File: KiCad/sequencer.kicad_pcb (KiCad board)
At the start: 2 copper layers, 79.9 x 100 mm, 125 parts, among them J1 CLOCK OUT, J2 GATE OUT, J3 CLOCK IN, J4 CV OUT, J5 RESET, J6 10-pin power header, Q1 BC848W, Q2 MMBT3904, Q3 MMBT3904, Q4 MMBT3904, Q5 MMBT3904, Q6 MMBT3904, Q7 MMBT3904, Q8 MMBT3904, Q9 MMBT3904, SW1 SW_Nidec_CAS-120A1, SW2 Step1, U1 TL074, U2 CD4017BE

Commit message: placing layout frontview
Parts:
- RV10, RV11, RV3, RV4, RV5, RV6, RV7, RV8, RV9: footprint Eurorack:RD901F -> Eurorack:RD901F_1
- SW2: value Step1 -> ~
- moved J1 48.1 mm to (118.5, 117.3), turned to 180 degrees
- moved J5 23.2 mm to (62.6, 132.0), turned to 180 degrees
- moved J6 22.6 mm to (85.9, 71.0)
- moved U1 20.7 mm to (84.0, 107.8)
- moved J2 18.6 mm to (118.5, 132.0), turned to 180 degrees
- moved RV1 16.7 mm to (102.8, 106.3), turned to -90 degrees
- moved U2 15.0 mm to (61.2, 113.9)
- moved RV2 13.7 mm to (120.4, 106.3), turned to -90 degrees
- moved S1 9.36 mm to (89.1, 133.0)
- moved J3 9.29 mm to (49.4, 132.0), turned to 180 degrees
- moved J4 6.77 mm to (105.3, 132.0), turned to 180 degrees
- moved RV3 6.69 mm to (56.0, 117.2), turned to 90 degrees
- moved SW5 6.62 mm to (112.0, 46.8)
- moved D28 5.85 mm to (110.7, 76.3)
- moved SW7 5.77 mm to (74.7, 105.1)
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
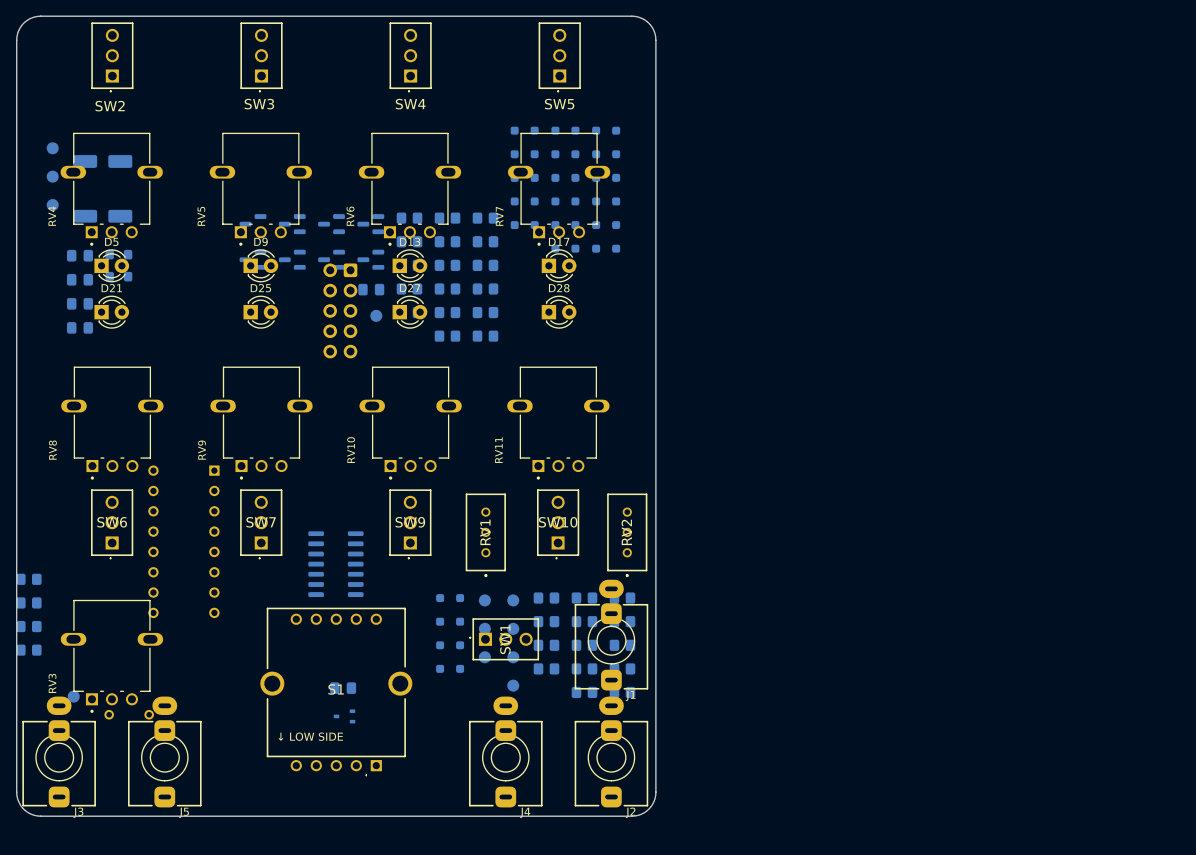
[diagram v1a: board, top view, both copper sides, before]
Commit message: fixing some errors in schematics; first component placement
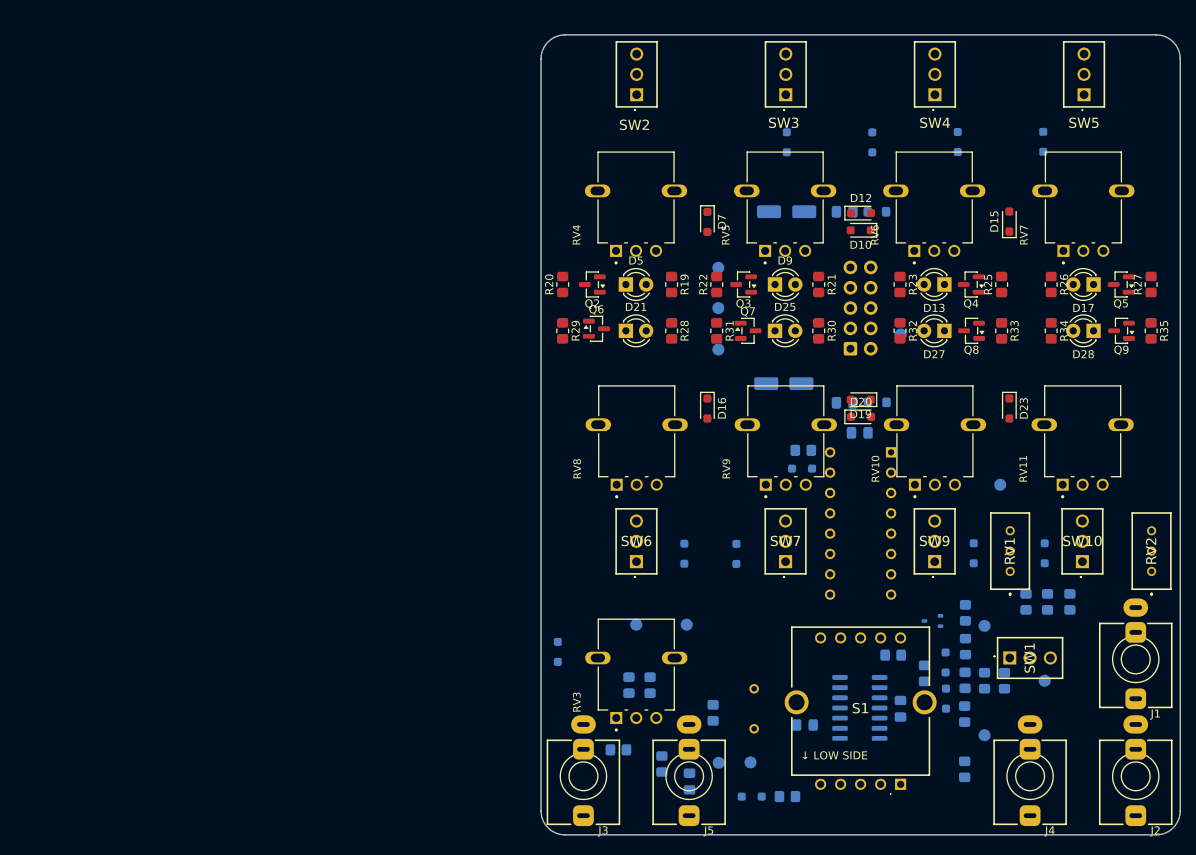
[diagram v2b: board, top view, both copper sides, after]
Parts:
- D10, D12, D15, D16, D19, D20, D23, D7, Q2, Q3, Q4, Q5, Q6, Q7, Q8, Q9, R19, R20, R21, R22, R23, R25, R26, R27, R28, R29, R30, R31, R32, R33, R34, R35: moved to F.Cu
- R13: value 51k -> 18k
- moved C7 114.4 mm to (154.6, 125.9), turned to -90 degrees
- moved Q9 108.9 mm to (182.2, 78.6)
- moved C8 103.3 mm to (142.7, 127.9), turned to 0 degrees
- moved Q5 98.7 mm to (182.2, 72.8)
- moved C5 96.8 mm to (147.6, 87.6)
- moved FB2 96.1 mm to (151.7, 87.6)
- moved C3 95.8 mm to (147.6, 63.7)
- moved FB1 94.9 mm to (151.6, 63.7), turned to 0 degrees
- moved R35 92.7 mm to (185.9, 78.6), turned to -90 degrees
- moved Q8 90.8 mm to (163.5, 78.6)
- moved R27 88.0 mm to (185.9, 72.8), turned to 90 degrees
- moved C6 87.7 mm to (140.0, 85.2), turned to 0 degrees
- moved R15 87.1 mm to (131.2, 126.4), turned to -90 degrees
- moved C4 85.7 mm to (140.4, 63.7)
- moved TP11 85.1 mm to (131.8, 80.9)
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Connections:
- D10 pad 2: GND -> Net-(D10-A)
- D11 pad 2: /CD4017BE/EXTERNAL RESET -> Net-(D11-A)
- D12 pad 2: GND -> Net-(D12-A)
- D15 pad 2: GND -> Net-(D15-A)
- D16 pad 2: GND -> Net-(D16-A)
- D19 pad 2: GND -> Net-(D19-A)
- D20 pad 2: GND -> Net-(D20-A)
- D23 pad 2: GND -> Net-(D23-A)
- FB1 pad 2: Net-(J6-Pin_10) -> +12V
- FB2 pad 2: Net-(J6-Pin_1) -> -12V
- J6 pad 1: Net-(J6-Pin_1) -> -12V
- J6 pad 10: Net-(J6-Pin_10) -> +12V
- J6 pad 2: Net-(J6-Pin_1) -> -12V
- J6 pad 9: Net-(J6-Pin_10) -> +12V
- RV10 pad 2: GND -> Net-(D20-A)
- RV11 pad 2: GND -> Net-(D23-A)
- RV5 pad 2: GND -> Net-(D10-A)
- RV6 pad 2: GND -> Net-(D12-A)
- RV7 pad 2: GND -> Net-(D15-A)
- RV8 pad 2: GND -> Net-(D16-A)
- RV9 pad 2: GND -> Net-(D19-A)
- S1 pad 1: /CD4017BE/EXTERNAL RESET -> Net-(D11-A)
- S1 pad 10: /CD4017BE/EXTERNAL RESET -> Net-(D11-A)

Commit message: connecting all components and adding copper layers, vias tracks…
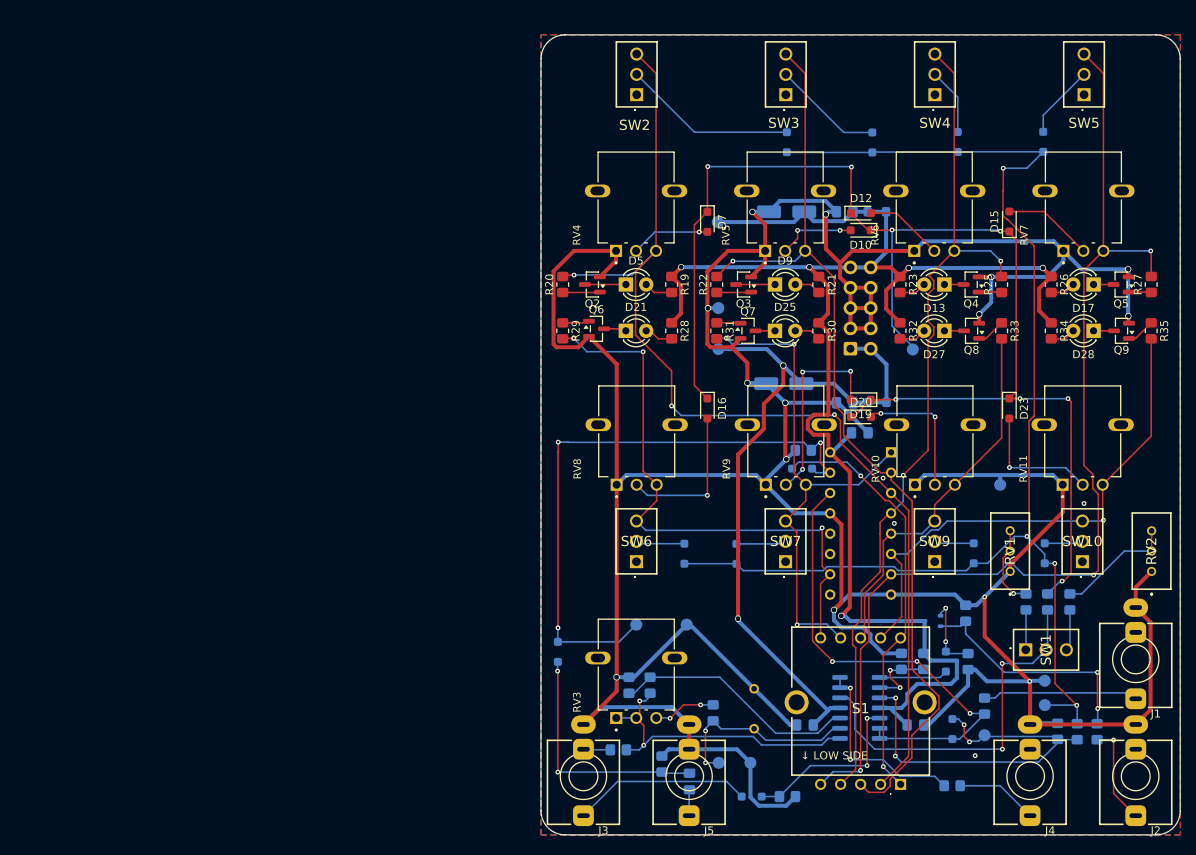
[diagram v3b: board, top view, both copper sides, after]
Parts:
- moved R3 13.2 mm to (179.2, 128.7)
- moved R1 13.2 mm to (176.7, 128.7)
- moved R4 13.2 mm to (174.2, 128.7)
- moved TP2 12.4 mm to (172.6, 125.4)
- moved TP9 5.72 mm to (131.7, 65.0)
- moved D2 3.89 mm to (161.1, 128.4)
- moved C7 2.76 mm to (156.5, 127.9), turned to 0 degrees
- moved R8 2.68 mm to (165.1, 125.5)
- moved R10 2.57 mm to (161.1, 135.5), turned to 180 degrees
- moved TP12 2.41 mm to (156.1, 80.9)
- moved SW1 2.25 mm to (170.3, 118.5)
- moved R6 1.90 mm to (163.0, 120.0), turned to 90 degrees
- moved R2 1.51 mm to (157.5, 119.9), turned to -90 degrees
- moved R5 1.30 mm to (154.7, 119.9), turned to -90 degrees
- moved D1 0.11 mm to (160.3, 120.0)
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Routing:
- net GND: track 0.00 -> 516.2 mm, vias 0 -> 18
- net +12V: track 0.00 -> 193.2 mm, vias 0 -> 5
- net /CD4017BE/CV OUT: track 0.00 -> 168.1 mm, vias 0 -> 8
- net /CD4017BE/GATE OUT: track 0.00 -> 162.3 mm, vias 0 -> 4
- net /CD4017BE/Count3: track 0.00 -> 135.5 mm, vias 0 -> 3
- net /CD4017BE/Count0: track 0.00 -> 133.3 mm, vias 0 -> 3
- net /CD4017BE/Count1: track 0.00 -> 119.7 mm, vias 0 -> 1
- net /CD4017BE/Count2: track 0.00 -> 108.0 mm, vias 0 -> 2
- net -12V: track 0.00 -> 88.2 mm, vias 0 -> 2
- net /CD4017BE/EXTERNAL RESET: track 0.00 -> 76.2 mm, vias 0 -> 3
- net /CD4017BE/Count4: track 0.00 -> 72.2 mm, vias 0 -> 3
- net /CD4017BE/Count5: track 0.00 -> 65.9 mm, vias 0 -> 3
- net /CD4017BE/Count7: track 0.00 -> 65.6 mm, vias 0 -> 1
- net /CD4017BE/EXTERNAL CLOCK: track 0.00 -> 60.5 mm, vias 0 -> 3
- net Net-(D11-A): track 0.00 -> 52.8 mm, vias 0 -> 2
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- added copper zone on B.Cu, net GND
- added copper zone on F.Cu, net GND

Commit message: rerouting and editing silkscreen
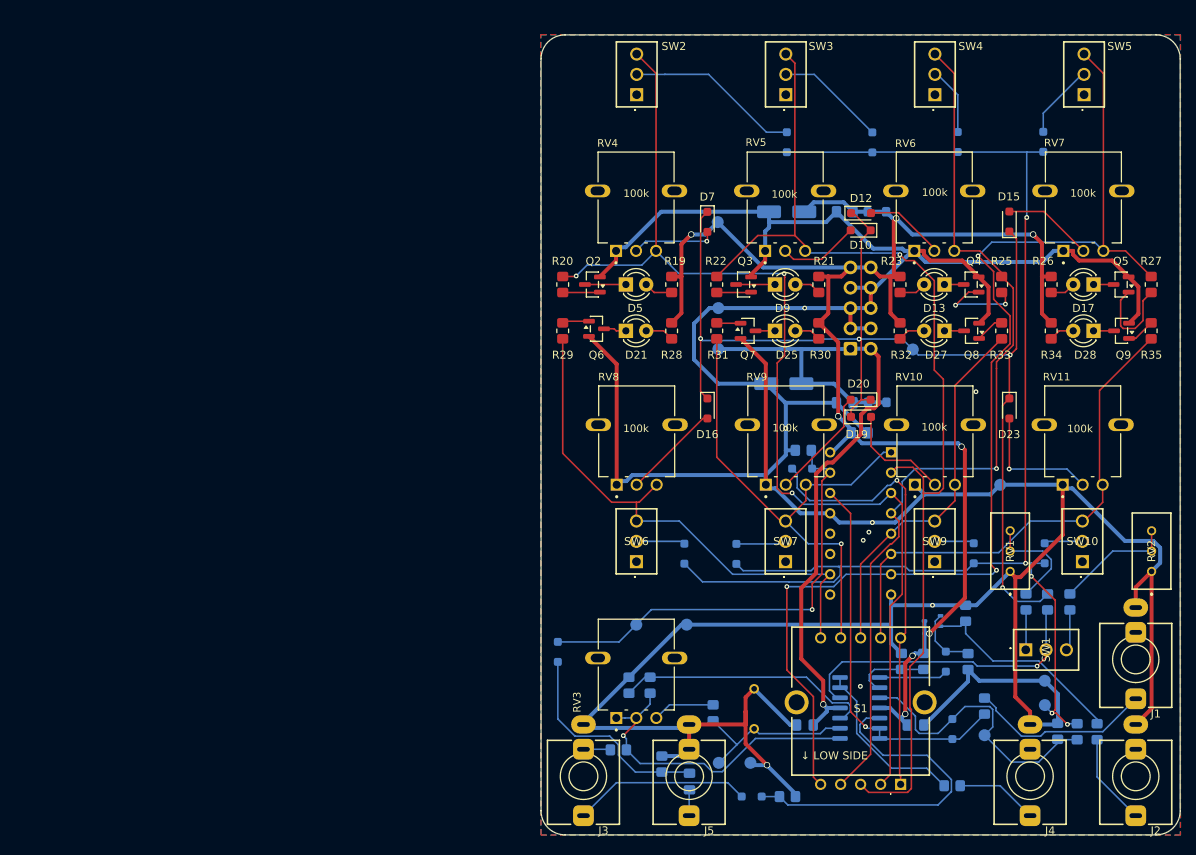
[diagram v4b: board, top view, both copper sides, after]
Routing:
- net /CD4017BE/CV OUT: track 168.1 -> 145.2 mm, vias 8 -> 4
- net Net-(D3-K): track 22.3 -> 44.0 mm, vias 2 -> 0
- net /CD4017BE/EXTERNAL RESET: track 76.2 -> 56.3 mm, vias 3 -> 1
- net /CD4017BE/Count1: track 119.7 -> 136.0 mm
- net Net-(D2-A): track 49.6 -> 36.6 mm, vias 4 -> 0
- net /CD4017BE/EXTERNAL CLOCK: track 60.5 -> 48.6 mm, vias 3 -> 1
- net Net-(D19-A): track 24.7 -> 14.0 mm, vias 3 -> 0
- net /CD4017BE/Count3: track 135.5 -> 145.4 mm
- net Net-(Q4-B): track 2.89 -> 12.3 mm, vias 0 -> 2
- net Net-(Q5-B): track 2.84 -> 11.9 mm
- net /CD4017BE/GATE OUT: track 162.3 -> 171.2 mm, vias 4 -> 5
- net Net-(SW1-B): track 46.7 -> 38.1 mm, vias 2 -> 1
- net GND: track 516.2 -> 523.0 mm, vias 18 -> 9
- net Net-(D16-A): track 19.0 -> 12.3 mm, vias 1 -> 0
- net /CD4017BE/Count2: track 108.0 -> 113.0 mm, vias 2 -> 1
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
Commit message: re-placing components; optimizing text on silkscreen
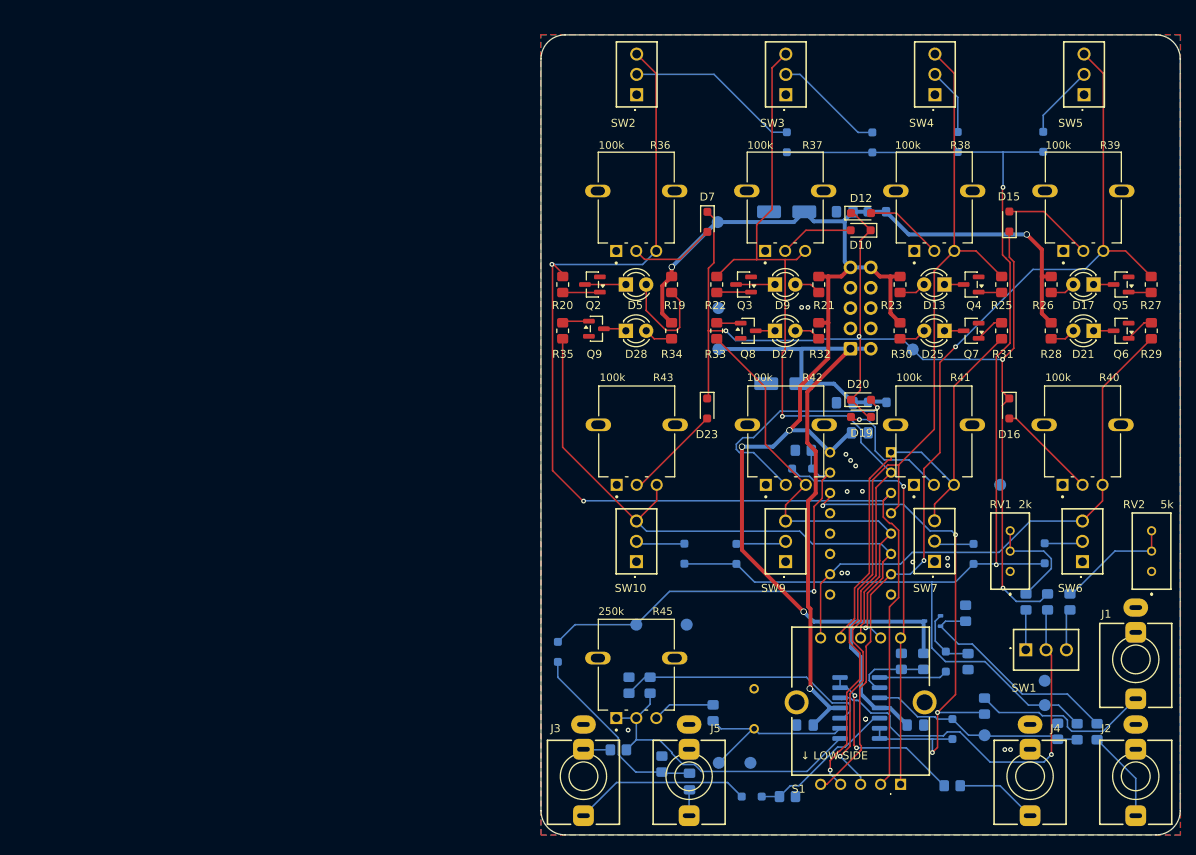
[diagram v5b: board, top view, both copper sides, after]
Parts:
- removed RV10, RV11, RV4, RV5, RV6, RV7, RV8, RV9: 100k, Eurorack:RD901F_1
- removed RV3: 250k, Eurorack:RD901F_1
- removed U2: CD4017BE, Eurorack:CD4017BE THT
- added R36: 100k, Eurorack:Potentiometer_Alpha_RD901F_Vertical_Alt, F.Cu at (121.6, 61.1)
- added R37: 100k, Eurorack:Potentiometer_Alpha_RD901F_Vertical_Alt, F.Cu at (140.2, 61.1)
- added R38: 100k, Eurorack:Potentiometer_Alpha_RD901F_Vertical_Alt, F.Cu at (158.8, 61.1)
- added R39: 100k, Eurorack:Potentiometer_Alpha_RD901F_Vertical_Alt, F.Cu at (177.5, 61.1)
- added R40: 100k, Eurorack:Potentiometer_Alpha_RD901F_Vertical_Alt, F.Cu at (177.4, 90.4)
- added R41: 100k, Eurorack:Potentiometer_Alpha_RD901F_Vertical_Alt, F.Cu at (158.8, 90.4)
- added R42: 100k, Eurorack:Potentiometer_Alpha_RD901F_Vertical_Alt, F.Cu at (140.3, 90.4)
- added R43: 100k, Eurorack:Potentiometer_Alpha_RD901F_Vertical_Alt, F.Cu at (121.6, 90.4)
- added R45: 250k, Eurorack:Potentiometer_Alpha_RD901F_Vertical_Alt, F.Cu at (121.6, 119.5)
- added U3: CD4017BE, Eurorack:IC_DIP-16_CD4017BE_THT, B.Cu at (145.8, 111.6)
- C2: footprint Eurorack:Kemet Film Cap -> Eurorack:Capacitor_Film_KEMET_R82DC4100AA60J_THT
- RV1, RV2: footprint Eurorack:3296W1503LF -> Eurorack:Trimmer_Bourns_3296W_50k_THT
- S1: value SR1712F-0108-20F0A-N9-N-027 -> Switch_Rotary_Alpha_SR1712F_1P8T; footprint Eurorack:1 Pole 8 Step Switch Alpha -> Eurorack:Switch_Rotary_Alpha_SR1712F_1P8T
- SW1, SW10, SW2, SW3, SW4, SW5, SW6, SW7, SW9: footprint Eurorack:2MS1T1B1M2QES -> Eurorack:Switch_Toggle_Dailywell_MS1T1B1M2QES_SPDT
- moved R29 73.6 mm to (186.0, 78.6)
- moved R35 73.6 mm to (112.4, 78.6)
- moved Q9 65.6 mm to (116.6, 78.3), turned to 0 degrees
- moved Q6 65.6 mm to (182.2, 78.6), turned to 180 degrees
- moved D21 58.5 mm to (178.7, 78.6), turned to 180 degrees
- moved D28 58.5 mm to (120.3, 78.6), turned to 0 degrees
- moved SW6 55.8 mm to (177.3, 107.5)
- moved SW10 55.7 mm to (121.6, 107.5)
- moved R34 47.5 mm to (126.0, 78.6)
- moved R28 47.4 mm to (173.4, 78.6)
- moved D22 45.0 mm to (172.6, 106.4)
- moved D29 45.0 mm to (127.6, 106.5)
- moved D23 37.8 mm to (130.4, 88.3)
- moved D16 37.7 mm to (168.2, 88.3)
- moved R33 35.6 mm to (131.6, 78.6)
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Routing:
- net GND: track 523.0 -> 0.00 mm, vias 9 -> 17
- net /CD4017BE/Count3: track 145.4 -> 120.1 mm, vias 3 -> 2
- net Net-(D3-K): track 44.0 -> 18.8 mm
- net /CD4017BE/EXTERNAL CLOCK: track 48.6 -> 66.7 mm, vias 1 -> 4
- net Net-(D20-A): track 13.7 -> 29.5 mm, vias 0 -> 1
- net /CD4017BE/Count1: track 136.0 -> 120.6 mm, vias 1 -> 2
- net /CD4017BE/Count7: track 63.4 -> 78.7 mm, vias 0 -> 1
- net /CD4017BE/Count0: track 136.9 -> 150.4 mm, vias 3 -> 2
- net Net-(SW1-B): track 38.1 -> 50.2 mm
- net /CD4017BE/Count6: track 47.0 -> 56.9 mm
- net Net-(D5-A): track 3.59 -> 13.4 mm
- net Net-(D2-A): track 36.6 -> 26.9 mm
- net Net-(Q4-B): track 12.3 -> 2.89 mm, vias 2 -> 0
- net Net-(Q5-B): track 11.9 -> 2.84 mm
- net /CD4017BE/GATE OUT: track 171.2 -> 162.2 mm, vias 5 -> 2
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
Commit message: changing position on silkscreen
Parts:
- added REF**: LayerMarker_2_3.81x2.54mm_TextH1mm_P1.27mm, Symbol:LayerMarker_2_3.81x2.54mm_TextH1mm_P1.27mm, F.Cu at (113.5, 46.4)
